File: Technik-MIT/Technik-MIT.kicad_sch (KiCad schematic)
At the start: 133 parts, among them J1 USB_C_Receptacle_USB2.0, SW1 SW_Push, SW10 SW_Push, SW11 SW_Push, SW12 SW_Push, SW13 SW_Push, SW14 SW_Push, SW15 SW_Push, SW16 SW_Push, SW17 SW_Push, SW18 SW_Push, SW19 SW_Push, SW2 SW_Push, SW20 SW_Push, SW21 SW_Push, SW22 SW_Push, SW23 SW_Push, SW24 SW_Push, SW25 SW_Push, SW26 SW_Push, SW27 SW_Push, SW28 SW_Push, SW29 SW_Push, SW3 SW_Push, SW30 SW_Push, SW31 SW_Push, SW32 SW_Push, SW33 SW_Push, SW34 SW_Push, SW35 SW_Push, SW36 SW_Push, SW37 SW_Push, SW38 SW_Push, SW39 SW_Push, SW4 SW_Push, SW40 SW_Push, SW41 SW_Push, SW42 SW_Push, SW43 SW_Push, SW44 SW_Push, SW45 SW_Push, SW46 SW_Push, SW47 SW_Push, SW48 RESET, SW5 SW_Push, SW6 SW_Push, SW7 SW_Push, SW8 SW_Push, SW9 SW_Push, U1 USBLC6-2SC6, U2 TVS0500DRV, U3 AP2127N-3.3, U4 W25Q32JVSS, U5 RP2040, Y1 Crystal_GND24

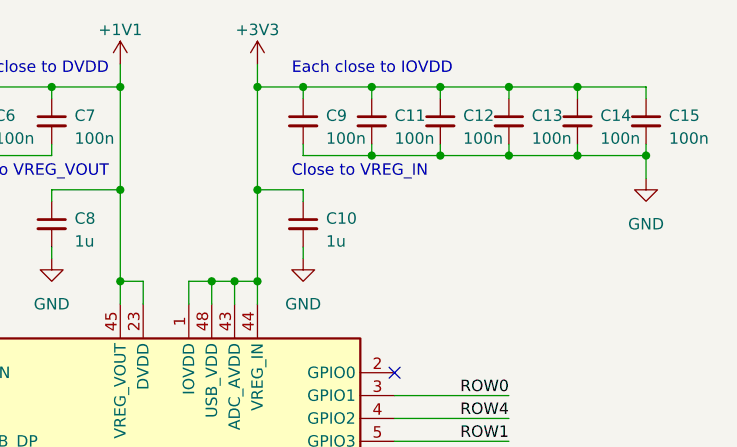
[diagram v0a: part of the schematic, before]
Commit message: Finalizing PCB layout for print
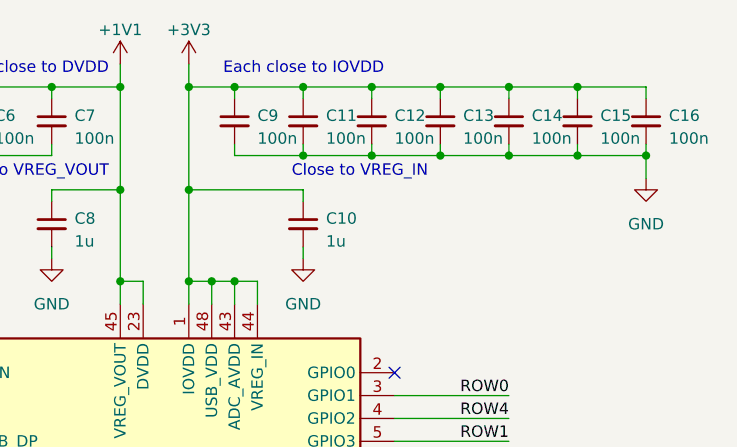
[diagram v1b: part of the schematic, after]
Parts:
- added C16: 100n, Capacitor_SMD:C_0402_1005Metric, symbol Device:C_Small
- SW40: footprint Technik-MIT:ChocV1_Hotswap -> Technik-MIT:ChocV1_Hotswap_WO_UpperRight
- SW44: footprint Technik-MIT:ChocV1_Hotswap -> Technik-MIT:ChocV1_Hotswap_WO_UpperLeft
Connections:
- net +3V3: now also C16.1
- net GND: now also C16.2
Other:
- moved on the sheet: C11, C12, C13, C14, C15, C9

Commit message: Changed PCB layout & schematics for cheaper production at JLCPCB
Used available basic parts alternatives
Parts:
- removed U1: USBLC6-2SC6, Package_TO_SOT_SMD:SOT-23-6, symbol Power_Protection:USBLC6-2SC6
- removed U2: TVS0500DRV, Package_SON:WSON-6-1EP_2x2mm_P0.65mm_EP1x1.6mm, symbol Power_Protection:TVS0500DRV
- removed U3: AP2127N-3.3, Package_TO_SOT_SMD:SOT-23, symbol Regulator_Linear:AP2127N-3.3
- removed U4: W25Q32JVSS, Package_SO:SOIC-8_5.23x5.23mm_P1.27mm, symbol Memory_Flash:W25Q32JVSS
- added D48: SMAJ5.0A, Diode_SMD:D_SMA, symbol Diode:Z1SMAxxx
- added U1: AMS1117-3.3, Package_TO_SOT_SMD:SOT-223-3_TabPin2, symbol Regulator_Linear:AMS1117-3.3
- added U2: W25Q128JVS, Package_SO:SOIC-8_5.23x5.23mm_P1.27mm, symbol Memory_Flash:W25Q128JVS
- added U3: ESDS302, Package_TO_SOT_SMD:SOT-23-5, symbol Technik-MIT:ESDS302
- C2: value 1u -> 22u; footprint Capacitor_SMD:C_0402_1005Metric -> Capacitor_SMD:C_0603_1608Metric
- C4, C5: value 27p -> 33p
- DIP1: LCSC (none) -> C431541
- J1: LCSC (none) -> C3019717
- R4, R5: footprint Resistor_SMD:R_0402_1005Metric -> Resistor_SMD:R_0603_1608Metric
- SW48: footprint Button_Switch_SMD:SW_SPST_B3U-1000P -> Button_Switch_SMD:SW_SPST_TL3342; LCSC (none) -> C318884
- Y1: LCSC (none) -> C9002
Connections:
- net +3V3: now also U1.2 (VO), U2.8 (VCC)
- net GND: now also D48.2 (A), U1.1 (GND), U2.4 (GND), U3.2 (GND)
- net QSPI_SCLK: now also U2.6 (CLK)
- net QSPI_SD0: now also U2.5 (DI(IO0))
- net QSPI_SD1: now also U2.2 (DO(IO1))
- net QSPI_SD2: now also U2.3 (IO2)
- net QSPI_SD3: now also U2.7 (IO3)
- net QSPI_SS: now also U2.1 (~{CS})
- net USB_D+: now also J1.A6 (D+), J1.B6 (D+), U3.3 (NC), U3.4 (I/O1)
- net USB_D-: now also J1.A7 (D-), J1.B7 (D-), U3.1 (NC), U3.5 (I/O2)
- net VBUS: now also D48.1 (K), U1.3 (VI)
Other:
- moved on the sheet: C1, C2
